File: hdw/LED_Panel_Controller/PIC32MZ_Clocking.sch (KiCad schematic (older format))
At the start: 16 parts

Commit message: lots of schematic progress
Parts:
- removed C? (x2): 0.1uF, Capacitors_SMD:C_0402, symbol Custom_Library:C_Custom
- removed C? (x2): 1nF, Capacitors_SMD:C_0402, symbol Custom_Library:C_Custom
- removed C? (x2): 10nF, Capacitors_SMD:C_0402, symbol Custom_Library:C_Custom
- added C? (x2): 0.1uF, Capacitors_SMD:C_0402, symbol Custom_Library:C_Custom
- added C? (x2): 10uF, Capacitors_SMD:C_0402, symbol Custom_Library:C_Custom
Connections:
- net GND: now also C?.2, C?.2, C?.2, C?.2
- net at L?.1, X?.4 (Vdd): now also C?.1, C?.1; no longer X?.1 (EN) (x2)
- new net POS3P3_PGOOD: X?.1 (EN), X?.1 (EN)

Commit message: made a lot more schematic progress
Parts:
- added C?: 0.1uF, Capacitors_SMD:C_0402, symbol Custom_Library:C_Custom
- added R?: 10k, Resistors_SMD:R_0402, symbol Custom_Library:R_Custom
- added U?: 74LVC1G97, Package_TO_SOT_SMD:SOT-363_SC-70-6, symbol Custom_Library:74LVC1G97_Power_BUF
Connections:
- net +3V3: now also C?.1, U?.5 (VCC)
- net GND: now also C?.2, R?.2, U?.2 (GND), U?.3 (GND), U?.6 (GND)
- net POS3P3_PGOOD: now also U?.1; no longer X?.1 (EN), X?.1 (EN)
- new net PIC32MZ_CLK_EN: R?.1, U?.4, X?.1 (EN), X?.1 (EN)
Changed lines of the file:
@@
 Wire Wire Line
 	5510 3850 5510 4450
-Text GLabel 5210 2700 0    50   Input ~ 0
-POS3P3_PGOOD
-Text GLabel 5210 4750 0    50   Input ~ 0
+Text GLabel 1680 2700 0    50   Input ~ 0
 POS3P3_PGOOD
 Wire Wire Line
@@
 	6820 3850 6820 3930
 Connection ~ 6120 3850
+$Comp
+L Custom_Library:C_Custom C?
+U 1 1 601DF015
+P 1870 2010
+AR Path="/5BAAE1F3/601DF015" Ref="C?"  Part="1"
+AR Path="/5BAAE1CB/601DF015" Ref="C?"  Part="1"
+AR Path="/5BE48F98/601DF015" Ref="C?"  Part="1"
+AR Path="/5CAD2D97/601DF015" Ref="C?"  Part="1"
+AR Path="/5CB7A8BC/601DF015" Ref="C?"  Part="1"
+AR Path="/5E6AF016/601DF015" Ref="C?"  Part="1"
+AR Path="/5EAE4AE4/601DF015" Ref="C?"  Part="1"
+AR Path="/5F582E50/601DF015" Ref="C?"  Part="1"
+AR Path="/5F5829C2/601DF015" Ref="C?"  Part="1"
+F 0 "C?" H 1895 2110 50  0000 L CNN
+F 1 "0.1uF" H 1895 1910 50  0000 L CNN
+F 2 "Capacitors_SMD:C_0402" H 1908 1860 50  0001 C CNN
+F 3 "" H 1895 2110 50  0001 C CNN
+F 4 "490-10701-1-ND" H 2295 2510 60  0001 C CNN "Digi-Key PN"
+F 5 "0402" H 1720 2110 50  0000 R CNN "display_footprint"
+F 6 "50V" H 1720 2010 50  0000 R CNN "Voltage"
+F 7 "X7R" H 1720 1910 50  0000 R CNN "Dielectric"
+	1    1870 2010
+	-1   0    0    -1
+$EndComp
+$Comp
+L power:+3.3V #PWR?
+U 1 1 601DF01B
+P 1870 1860
+AR Path="/5F582E50/601DF01B" Ref="#PWR?"  Part="1"
+AR Path="/5F5829C2/601DF01B" Ref="#PWR?"  Part="1"
+F 0 "#PWR?" H 1870 1710 50  0001 C CNN
+F 1 "+3.3V" H 1870 2000 50  0000 C CNN
+F 2 "" H 1870 1860 50  0001 C CNN
+F 3 "" H 1870 1860 50  0001 C CNN
+	1    1870 1860
+	1    0    0    -1
+$EndComp
+$Comp
+L power:GND #PWR?
+U 1 1 601DF021
+P 1870 2160
+AR Path="/5F582E50/601DF021" Ref="#PWR?"  Part="1"
+AR Path="/5F5829C2/601DF021" Ref="#PWR?"  Part="1"
+F 0 "#PWR?" H 1870 1910 50  0001 C CNN
+F 1 "GND" H 1870 2010 50  0000 C CNN
+F 2 "" H 1870 2160 50  0001 C CNN
+F 3 "" H 1870 2160 50  0001 C CNN
+	1    1870 2160
+	1    0    0    -1
+$EndComp
+$Comp
+L power:+3.3V #PWR?
+U 1 1 601DF027
+P 1980 2600
+AR Path="/5F582E50/601DF027" Ref="#PWR?"  Part="1"
+AR Path="/5F5829C2/601DF027" Ref="#PWR?"  Part="1"
+F 0 "#PWR?" H 1980 2450 50  0001 C CNN
+F 1 "+3.3V" H 1980 2740 50  0000 C CNN
+F 2 "" H 1980 2600 50  0001 C CNN
+F 3 "" H 1980 2600 50  0001 C CNN
+	1    1980 2600
+	1    0    0    -1
+$EndComp
+$Comp
+L power:GND #PWR?
+U 1 1 601DF02D
+P 1980 2800
+AR Path="/5F582E50/601DF02D" Ref="#PWR?"  Part="1"
+AR Path="/5F5829C2/601DF02D" Ref="#PWR?"  Part="1"
+F 0 "#PWR?" H 1980 2550 50  0001 C CNN
+F 1 "GND" H 1980 2650 50  0000 C CNN
+F 2 "" H 1980 2800 50  0001 C CNN
+F 3 "" H 1980 2800 50  0001 C CNN
+	1    1980 2800
+	1    0    0    -1
+$EndComp
+$Comp
+L Custom_Library:74LVC1G97_Power_BUF U?
+U 1 1 601DFA25
+P 1980 2700
+F 0 "U?" H 2040 2850 50  0000 L CNN
+F 1 "74LVC1G97" H 2040 2550 50  0000 L CNN
+F 2 "Package_TO_SOT_SMD:SOT-363_SC-70-6" H 2030 2700 50  0001 C CNN
+F 3 "http://www.ti.com/lit/ds/symlink/sn74lvc1g97.pdf" H 2030 2700 50  0001 C CNN
+	1    1980 2700
+	1    0    0    -1
+$EndComp
+$Comp
+L Custom_Library:R_Custom R?
+U 1 1 601E190B
+P 2810 2930
+AR Path="/5BAAE1F3/601E190B" Ref="R?"  Part="1"
+AR Path="/5BAAE1DC/601E190B" Ref="R?"  Part="1"
+AR Path="/5BAAE16C/601E190B" Ref="R?"  Part="1"
+AR Path="/5BB844FD/601E190B" Ref="R?"  Part="1"
+AR Path="/5BF346B3/601E190B" Ref="R?"  Part="1"
+AR Path="/5CAD2D97/601E190B" Ref="R?"  Part="1"
+AR Path="/5CB7A8BC/601E190B" Ref="R?"  Part="1"
+AR Path="/5E01BCC3/601E190B" Ref="R?"  Part="1"
+AR Path="/5E697952/601E190B" Ref="R?"  Part="1"
+AR Path="/5EAE2F15/601E190B" Ref="R?"  Part="1"
+AR Path="/5F5829C2/601E190B" Ref="R?"  Part="1"
+F 0 "R?" H 2750 2930 50  0000 R CNN
+F 1 "10k" V 2810 2930 50  0000 C CNN
+F 2 "Resistors_SMD:R_0402" H 2810 2930 50  0001 C CNN
+F 3 "" H 2810 2930 50  0001 C CNN
+F 4 "0402" H 2880 3010 50  0000 L CNN "display_footprint"
+F 5 "1%" H 2880 2930 50  0000 L CNN "Tolerance"
+F 6 "1/16W" H 2880 2860 50  0000 L CNN "Wattage"
+F 7 "RMCF0402FT10K0CT-ND" H 2810 2930 50  0001 C CNN "Digi-Key PN"
+	1    2810 2930
+	-1   0    0    -1
+$EndComp
+$Comp
+L power:GND #PWR?
+U 1 1 601E2D03
+P 2810 3080
+AR Path="/5F582E50/601E2D03" Ref="#PWR?"  Part="1"
+AR Path="/5F5829C2/601E2D03" Ref="#PWR?"  Part="1"
+F 0 "#PWR?" H 2810 2830 50  0001 C CNN
+F 1 "GND" H 2810 2930 50  0000 C CNN
+F 2 "" H 2810 3080 50  0001 C CNN
+F 3 "" H 2810 3080 50  0001 C CNN
+	1    2810 3080
+	1    0    0    -1
+$EndComp
+Wire Wire Line
+	2810 2780 2810 2700
+Wire Wire Line
+	2810 2700 2230 2700
+Text GLabel 2890 2700 2    50   Output ~ 0
+PIC32MZ_CLK_EN
+Wire Wire Line
+	2890 2700 2810 2700
+Connection ~ 2810 2700
+Text GLabel 5210 2700 0    50   Input ~ 0
+PIC32MZ_CLK_EN
+Text GLabel 5210 4750 0    50   Input ~ 0
+PIC32MZ_CLK_EN
 $EndSCHEMATC

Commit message: added digikey pns, footprints, bom scrubbed
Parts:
- C? (x2): Digi-Key PN 490-13211-1-ND -> 1276-1451-1-ND
- R? (x2): Digi-Key PN (none) -> RMCF0402FT100RCT-ND
- U?: Digi-Key PN (none) -> 1727-1772-1-ND
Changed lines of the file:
@@
 F 5 "1%" V 6310 2700 50  0001 C CNN "Tolerance"
 F 6 "1/16W" V 6410 2700 50  0001 C CNN "Wattage"
-F 7 "" H 6410 3100 60  0001 C CNN "Digi-Key PN"
+F 7 "RMCF0402FT100RCT-ND" H 6410 3100 60  0001 C CNN "Digi-Key PN"
 	1    6110 2700
 	0    -1   1    0
@@
 F 5 "1%" V 6310 4750 50  0001 C CNN "Tolerance"
 F 6 "1/16W" V 6410 4750 50  0001 C CNN "Wattage"
-F 7 "" H 6410 5150 60  0001 C CNN "Digi-Key PN"
+F 7 "RMCF0402FT100RCT-ND" H 6410 5150 60  0001 C CNN "Digi-Key PN"
 	1    6110 4750
 	0    -1   1    0
@@
 F 5 "6.3V" H 6670 2030 50  0000 R CNN "Voltage"
 F 6 "X5R" H 6670 1930 50  0000 R CNN "Dielectric"
-F 7 "490-13211-1-ND" H 6820 2030 50  0001 C CNN "Digi-Key PN"
+F 7 "1276-1451-1-ND" H 6820 2030 50  0001 C CNN "Digi-Key PN"
 	1    6820 2030
 	1    0    0    -1
@@
 F 5 "6.3V" H 6670 4080 50  0000 R CNN "Voltage"
 F 6 "X5R" H 6670 3980 50  0000 R CNN "Dielectric"
-F 7 "490-13211-1-ND" H 6820 4080 50  0001 C CNN "Digi-Key PN"
+F 7 "1276-1451-1-ND" H 6820 4080 50  0001 C CNN "Digi-Key PN"
 	1    6820 4080
 	1    0    0    -1
@@
 F 2 "Package_TO_SOT_SMD:SOT-363_SC-70-6" H 2030 2700 50  0001 C CNN
 F 3 "http://www.ti.com/lit/ds/symlink/sn74lvc1g97.pdf" H 2030 2700 50  0001 C CNN
+F 4 "1727-1772-1-ND" H 1980 2700 50  0001 C CNN "Digi-Key PN"
 	1    1980 2700
 	1    0    0    -1

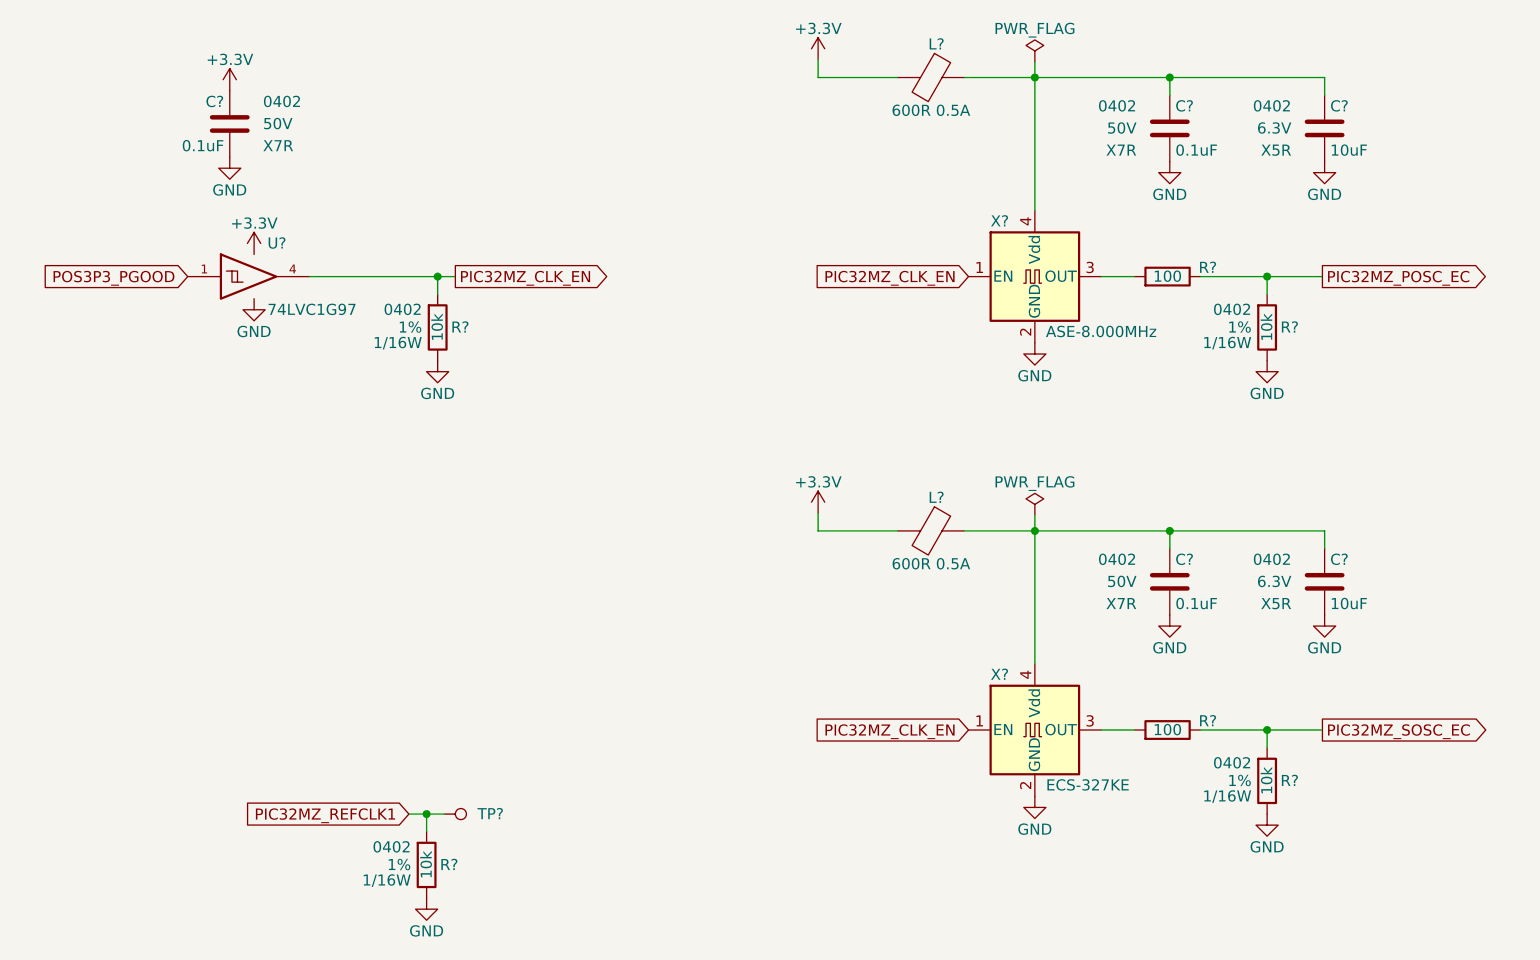
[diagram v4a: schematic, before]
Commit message: assigned I2C addresses
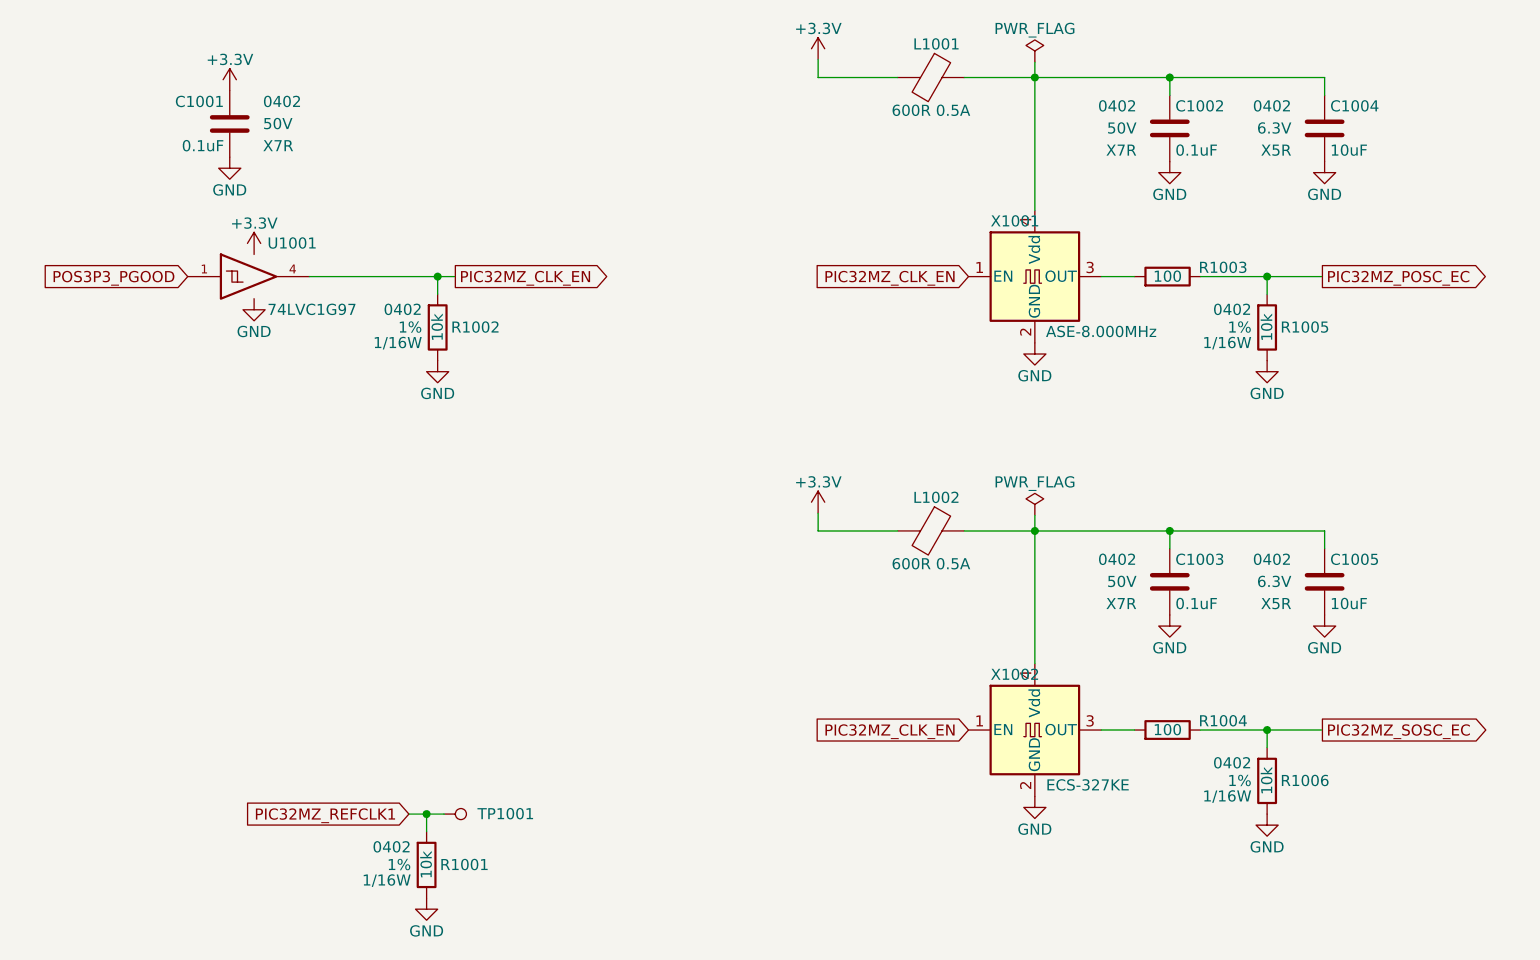
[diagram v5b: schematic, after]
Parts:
- gave numbers to parts that had none: 17

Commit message: reviewed schematic
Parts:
- R1003, R1004: value 100 -> 10; Digi-Key PN RMCF0402FT100RCT-ND -> RMCF0402FT10R0CT-ND
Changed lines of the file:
@@
 Sheet 10 34
 Title "LED Panel Controller"
-Date "2021-03-24"
+Date "2021-03-31"
 Rev "A"
 Comp "Drew Maatman"
@@
 	6560 2700 6560 2780
 Connection ~ 6560 2700
-$Comp
-L Custom_Library:R_Custom R?
-U 1 1 5E024C29
-P 6110 2700
-AR Path="/5BAAE2B6/5E024C29" Ref="R?"  Part="1"
-AR Path="/5BB6CF6D/5E024C29" Ref="R?"  Part="1"
-AR Path="/5BBE424C/5E024C29" Ref="R?"  Part="1"
-AR Path="/5BAAE1DC/5E024C29" Ref="R?"  Part="1"
-AR Path="/5CAD2DA3/5E024C29" Ref="R?"  Part="1"
-AR Path="/5E01BCC3/5E024C29" Ref="R?"  Part="1"
-AR Path="/5E697952/5E024C29" Ref="R?"  Part="1"
-AR Path="/5EAE2F15/5E024C29" Ref="R?"  Part="1"
-AR Path="/5F5829C2/5E024C29" Ref="R1003"  Part="1"
-F 0 "R1003" V 6070 2560 50  0000 R CNN
-F 1 "100" V 6110 2700 50  0000 C CNN
-F 2 "Resistors_SMD:R_0402" H 6110 2700 50  0001 C CNN
-F 3 "" H 6110 2700 50  0001 C CNN
-F 4 "0402" V 6210 2700 50  0001 C CNN "display_footprint"
-F 5 "1%" V 6310 2700 50  0001 C CNN "Tolerance"
-F 6 "1/16W" V 6410 2700 50  0001 C CNN "Wattage"
-F 7 "RMCF0402FT100RCT-ND" H 6410 3100 60  0001 C CNN "Digi-Key PN"
-	1    6110 2700
-	0    -1   1    0
-$EndComp
 Wire Wire Line
 	5960 2700 5810 2700
@@
 	6560 4750 6560 4830
 Connection ~ 6560 4750
-$Comp
-L Custom_Library:R_Custom R?
-U 1 1 5F689623
-P 6110 4750
-AR Path="/5BAAE2B6/5F689623" Ref="R?"  Part="1"
-AR Path="/5BB6CF6D/5F689623" Ref="R?"  Part="1"
-AR Path="/5BBE424C/5F689623" Ref="R?"  Part="1"
-AR Path="/5BAAE1DC/5F689623" Ref="R?"  Part="1"
-AR Path="/5CAD2DA3/5F689623" Ref="R?"  Part="1"
-AR Path="/5E01BCC3/5F689623" Ref="R?"  Part="1"
-AR Path="/5E697952/5F689623" Ref="R?"  Part="1"
-AR Path="/5EAE2F15/5F689623" Ref="R?"  Part="1"
-AR Path="/5F5829C2/5F689623" Ref="R1004"  Part="1"
-F 0 "R1004" V 6070 4610 50  0000 R CNN
-F 1 "100" V 6110 4750 50  0000 C CNN
-F 2 "Resistors_SMD:R_0402" H 6110 4750 50  0001 C CNN
-F 3 "" H 6110 4750 50  0001 C CNN
-F 4 "0402" V 6210 4750 50  0001 C CNN "display_footprint"
-F 5 "1%" V 6310 4750 50  0001 C CNN "Tolerance"
-F 6 "1/16W" V 6410 4750 50  0001 C CNN "Wattage"
-F 7 "RMCF0402FT100RCT-ND" H 6410 5150 60  0001 C CNN "Digi-Key PN"
-	1    6110 4750
-	0    -1   1    0
-$EndComp
 Wire Wire Line
 	5960 4750 5810 4750
@@
 Text GLabel 5210 4750 0    50   Input ~ 0
 PIC32MZ_CLK_EN
+$Comp
+L Custom_Library:R_Custom R?
+U 1 1 606585C6
+P 6110 2700
+AR Path="/5F5829A6/606585C6" Ref="R?"  Part="1"
+AR Path="/5F5829C2/606585C6" Ref="R1003"  Part="1"
+F 0 "R1003" V 6010 2700 50  0000 C CNN
+F 1 "10" V 6110 2700 50  0000 C CNN
+F 2 "Resistors_SMD:R_0402" H 6110 2700 50  0001 C CNN
+F 3 "" H 6110 2700 50  0001 C CNN
+F 4 "0402" V 6210 2700 50  0000 C CNN "display_footprint"
+F 5 "1%" V 6310 2700 50  0000 C CNN "Tolerance"
+F 6 "1/16W" V 6410 2700 50  0000 C CNN "Wattage"
+F 7 "RMCF0402FT10R0CT-ND" H 6410 3100 60  0001 C CNN "Digi-Key PN"
+	1    6110 2700
+	0    -1   -1   0
+$EndComp
+$Comp
+L Custom_Library:R_Custom R?
+U 1 1 60658A20
+P 6110 4750
+AR Path="/5F5829A6/60658A20" Ref="R?"  Part="1"
+AR Path="/5F5829C2/60658A20" Ref="R1004"  Part="1"
+F 0 "R1004" V 6010 4750 50  0000 C CNN
+F 1 "10" V 6110 4750 50  0000 C CNN
+F 2 "Resistors_SMD:R_0402" H 6110 4750 50  0001 C CNN
+F 3 "" H 6110 4750 50  0001 C CNN
+F 4 "0402" V 6210 4750 50  0000 C CNN "display_footprint"
+F 5 "1%" V 6310 4750 50  0000 C CNN "Tolerance"
+F 6 "1/16W" V 6410 4750 50  0000 C CNN "Wattage"
+F 7 "RMCF0402FT10R0CT-ND" H 6410 5150 60  0001 C CNN "Digi-Key PN"
+	1    6110 4750
+	0    -1   -1   0
+$EndComp
 $EndSCHEMATC

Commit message: added BOMs, some consolidation
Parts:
- C1001, C1002, C1003: Digi-Key PN 490-10701-1-ND -> 490-10698-1-ND
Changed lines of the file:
@@
 F 5 "50V" H 5970 2030 50  0000 R CNN "Voltage"
 F 6 "X7R" H 5970 1930 50  0000 R CNN "Dielectric"
-F 7 "490-10701-1-ND" H 2210 -4850 50  0001 C CNN "Digi-Key PN"
+F 7 "490-10698-1-ND" H 2210 -4850 50  0001 C CNN "Digi-Key PN"
 	1    6120 2030
 	1    0    0    -1
@@
 F 5 "50V" H 5970 4080 50  0000 R CNN "Voltage"
 F 6 "X7R" H 5970 3980 50  0000 R CNN "Dielectric"
-F 7 "490-10701-1-ND" H 2210 -2800 50  0001 C CNN "Digi-Key PN"
+F 7 "490-10698-1-ND" H 2210 -2800 50  0001 C CNN "Digi-Key PN"
 	1    6120 4080
 	1    0    0    -1
@@
 F 2 "Capacitors_SMD:C_0402" H 1908 1860 50  0001 C CNN
 F 3 "" H 1895 2110 50  0001 C CNN
-F 4 "490-10701-1-ND" H 2295 2510 60  0001 C CNN "Digi-Key PN"
+F 4 "490-10698-1-ND" H 2295 2510 60  0001 C CNN "Digi-Key PN"
 F 5 "0402" H 1720 2110 50  0000 R CNN "display_footprint"
 F 6 "50V" H 1720 2010 50  0000 R CNN "Voltage"
